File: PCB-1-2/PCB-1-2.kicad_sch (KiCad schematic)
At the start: 4 parts, among them U1 LTC1298IS8_PBF, U2 LTC1451IS8-PBF, U3 HI-3110PSIF, U4 FT231XS-R

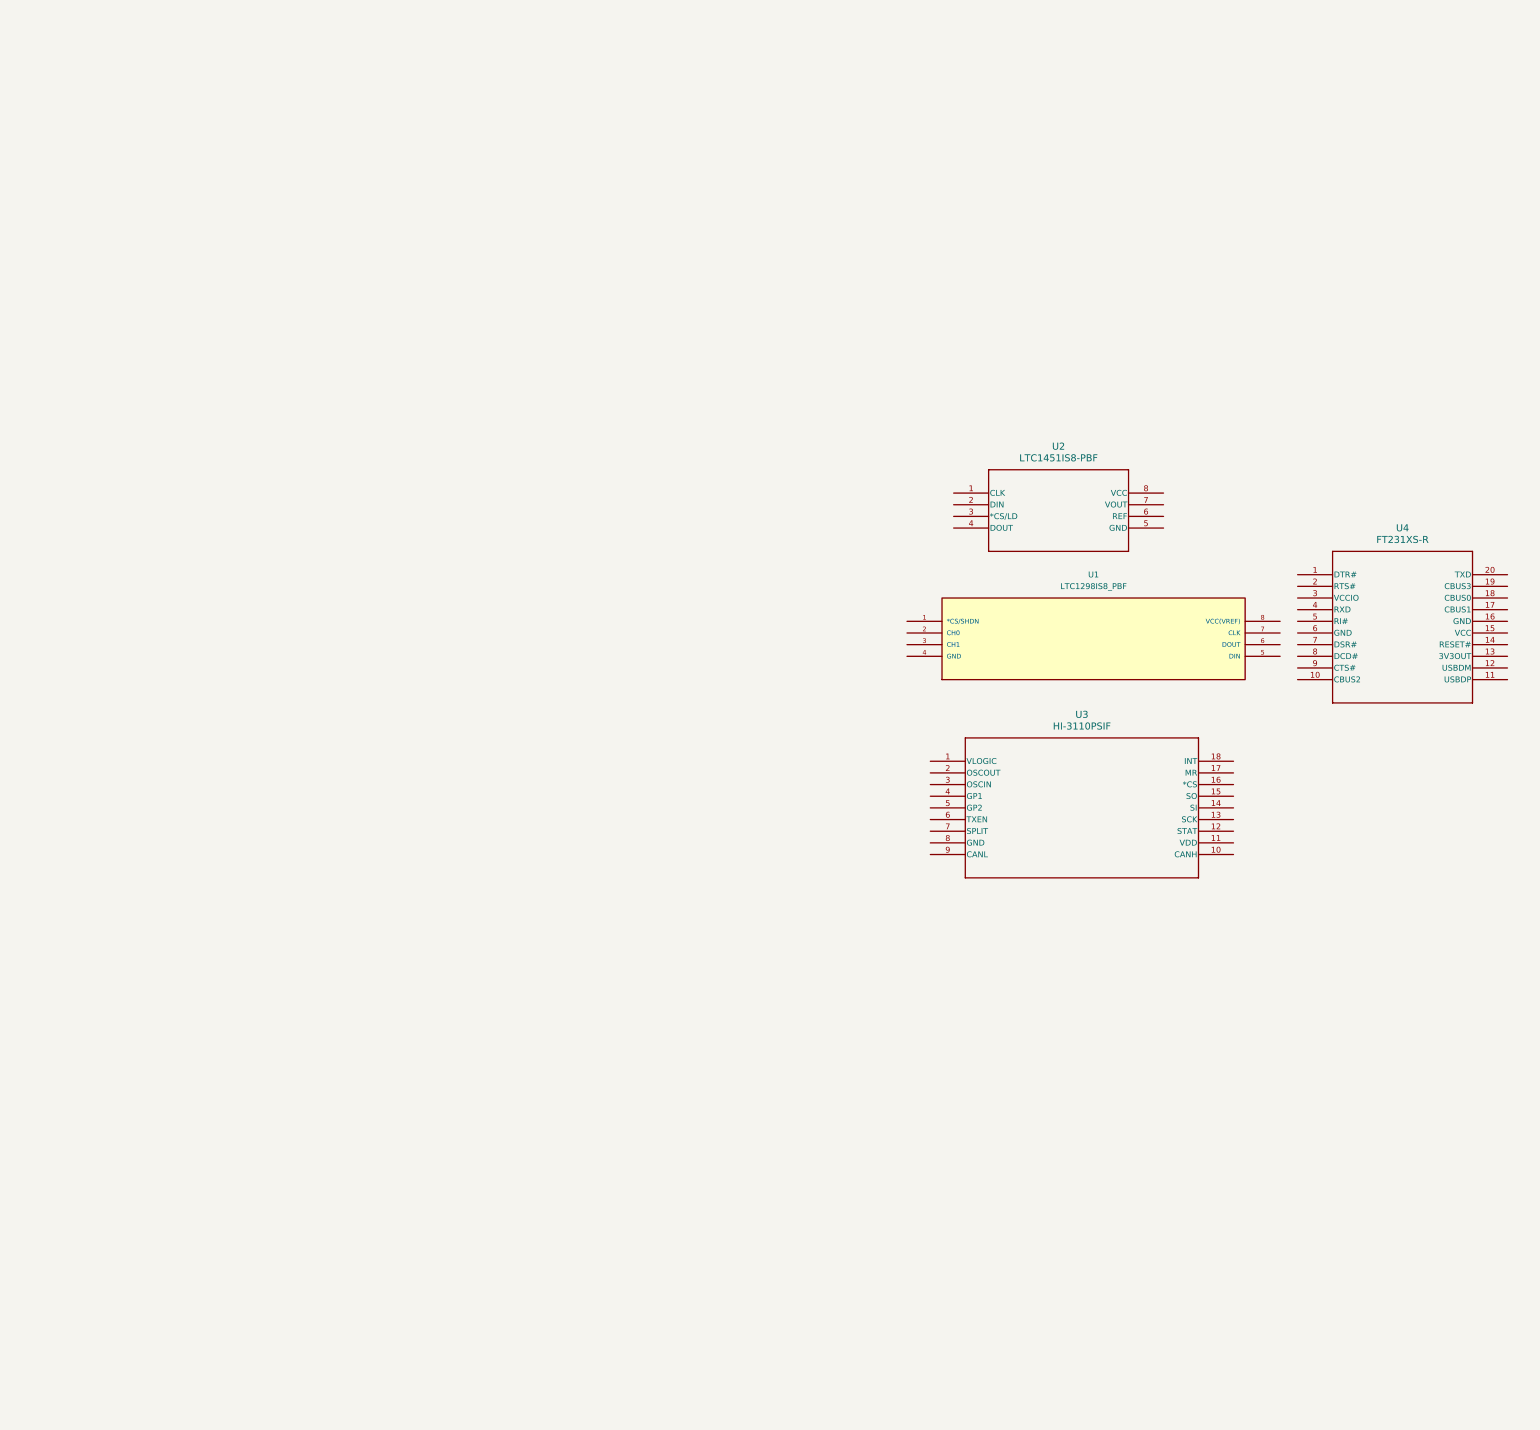
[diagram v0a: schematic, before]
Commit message: Added Schemaitic for ADC, DAC, USB-C. FT231 is still in progress
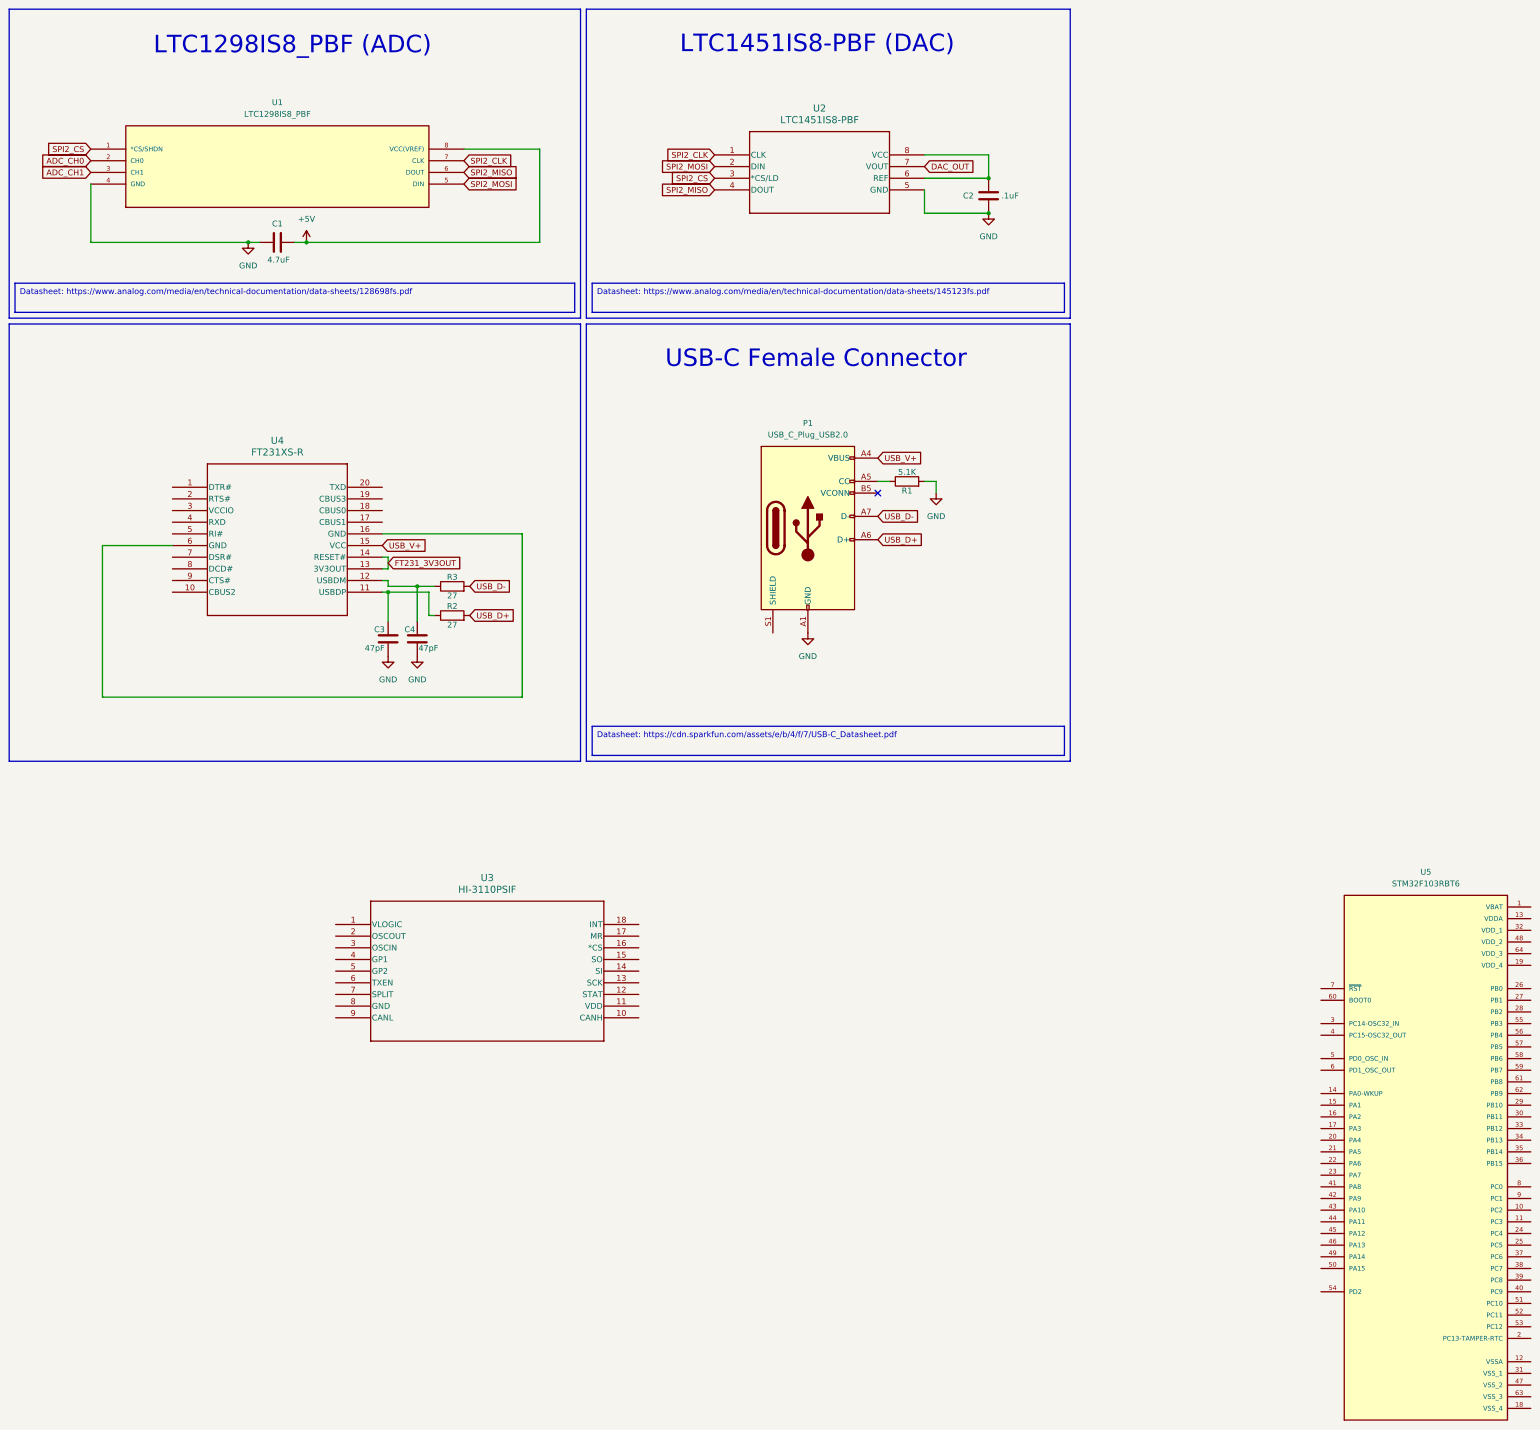
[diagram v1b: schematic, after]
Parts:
- added C1: 4.7uF, symbol Device:C
- added C2: .1uF, symbol Device:C
- added C3, C4: 47pF, symbol Device:C
- added P1: USB_C_Plug_USB2.0, symbol Connector:USB_C_Plug_USB2.0
- added R1: 5.1K, symbol Device:R
- added R2, R3: 27, symbol Device:R
- added U5: STM32F103RBT6, SDII LIB:QFP50P1200X1200X160-64N, symbol STM32F103RBT6:STM32F103RBT6
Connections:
- net SPI2_CLK: now reaches U2.1 (CLK)
- net SPI2_CLK: now also U1.7 (CLK)
- net SPI2_MOSI: now reaches U2.2 (DIN)
- net SPI2_MOSI: now also U1.5 (DIN)
- net SPI2_CS: now reaches U2.3 (*CS/LD)
- net SPI2_CS: now also U1.1 (*CS/SHDN)
- net SPI2_MISO: now reaches U2.4 (DOUT)
- net SPI2_MISO: now also U1.6 (DOUT)
- net GND: now reaches U2.5 (GND)
- net GND: now also U1.4 (GND), C1.1, C2.2, C3.2, C4.2, P1.A1 (GND), P1.A12 (GND), P1.B1 (GND), P1.B12 (GND), R1.2
- net at U2.6 (REF): now also U2.8 (VCC), C2.1
- net DAC_OUT: now reaches U2.7 (VOUT)
- net at U4.11 (USBDP): now also C3.1, R2.1
- net at U4.12 (USBDM): now also C4.1, R3.1
- net FT231_3V3OUT: now reaches U4.13 (3V3OUT)
- net FT231_3V3OUT: now also U4.14 (RESET#)
- net USB_V+: now reaches U4.15 (VCC)
- net USB_V+: now also P1.A4 (VBUS), P1.A9 (VBUS), P1.B4 (VBUS), P1.B9 (VBUS)
- net at U4.16 (GND): now also U4.6 (GND)
- net ADC_CH0: now reaches U1.2 (CH0)
- net ADC_CH1: now reaches U1.3 (CH1)
- net +5V: now reaches U1.8 (VCC(VREF))
- net +5V: now also C1.2
- new net: P1.A5 (CC), R1.1
- new net USB_D+: P1.A6 (D+), R2.2
- new net USB_D-: P1.A7 (D-), R3.2
- no-connect marks 0 -> 1
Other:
- note added: "LTC1298IS8_PBF (ADC)"
- note added: "LTC1451IS8-PBF (DAC)"
- note added: "USB-C Female Connector"
- moved on the sheet: U2, U3, U4

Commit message: Added misc components and added complimentary parts for the MCU
- Added the ADP7104 5v & 3.3V LDO's
- Added the Watchdog and connected it
- Added complimentary components for STM32
- Figured out the desired crystal and complimentary components
- Added Debug port for the ST-Link v3-MINIE
- Assigned footprints for all capacitors and most resistors
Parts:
- added C10, C11, C5, C7, C8, C9: 100nF, Capacitor_SMD:C_0805_2012Metric, symbol Device:C
- added C12: 10uF, Capacitor_SMD:C_0805_2012Metric, symbol Device:C
- added C13, C6: 10nF, Capacitor_SMD:C_0805_2012Metric, symbol Device:C
- added C14, C15: 1uF, Capacitor_SMD:C_0805_2012Metric, symbol Device:C
- added C16, C17: 10pF, Capacitor_SMD:C_0805_2012Metric, symbol Device:C
- added C18, C19: 2.2uF, Capacitor_SMD:C_0805_2012Metric, symbol Device:C
- added C20: .1uF, Capacitor_SMD:C_0805_2012Metric, symbol Device:C
- added FB1: FerriteBead, symbol Device:FerriteBead
- added FB2: 120R, symbol Device:FerriteBead
- added J1: Bus_PCI_Express_x8, Connector_PCBEdge:BUS_PCIexpress_x8, symbol Connector:Bus_PCI_Express_x8
- added J2: ST STDC14 (Debug Connector), FTSH-107-01-F-DV-K-P-TR:SAMTEC_FTSH-107-01-F-DV-K-P-TR, symbol STDC14 (STM32 Debug Conn):FTSH-107-01-F-DV-K-P-TR
- added R10, R5: 100k, Resistor_SMD:R_0805_2012Metric, symbol Device:R
- added R4: 22, symbol Device:R
- added R6, R8: 17.4k, Resistor_SMD:R_0805_2012Metric, symbol Device:R
- added R7: 5.6k, Resistor_SMD:R_0805_2012Metric, symbol Device:R
- added R9: 10k, Resistor_SMD:R_0805_2012Metric, symbol Device:R
- added U6: STWD100YNXWY3F, SDII LIB:SOT23-5_STM, symbol STWD100YNXWY3F (Watchdog):STWD100YNXWY3F
- added U7: ADP7104ACPZ-5V, SDII LIB:CP_8_5_ADI, symbol ADP7104 (LDO):ADP7104ACPZ-3.0-R7
- added U8: ADP7104ACPZ-3.3V, SDII LIB:CP_8_5_ADI, symbol ADP7104 (LDO):ADP7104ACPZ-3.0-R7
- added Y1: 8MHz Crystal, SDII LIB:XTAL_ABM3B-8.000MHZ-10-1-U-T, symbol ABM3B-8MHz (Crystal):ABM3B-8.000MHZ-10-1-U-T
- C1, C2, C3, C4: footprint (none) -> Capacitor_SMD:C_0805_2012Metric
- R1: footprint (none) -> Resistor_SMD:R_0805_2012Metric
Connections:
- net GND is gone; now on net +5V: C1.1, C2.2, C3.2, C4.2, P1.A1 (GND), P1.A12 (GND), P1.B1 (GND), P1.B12 (GND), R1.2, U1.4 (GND), U2.5 (GND)
- net +5V: now also U5.12 (VSSA), U5.18 (VSS_4), U5.31 (VSS_1), U5.47 (VSS_2), U5.60 (BOOT0), U5.63 (VSS_3), C10.1, C11.1, C12.1, C13.2, C14.2, C15.2, C16.2, C17.2, C18.1, C18.2, C19.2, C20.2, C7.1, C8.1, C9.1, J2.05 (GND), J2.07 (GND), J2.11 (GNDDETECT), R5.1, R6.2, R7.1, R9.1, U6.2 (GND), U7.1 (VOUT), U7.3 (GND), U7.6 (GND), U7.9 (EPAD), U8.3 (GND), U8.6 (GND), U8.9 (EPAD), Y1.2 (GND), Y1.4 (GND__1)
- net FT231_3V3OUT: now also U4.3 (VCCIO), C5.1
- net SPI2_CLK: now also U5.34 (PB13)
- net SPI2_MISO: now also U5.35 (PB14)
- net SPI2_MOSI: now also U5.36 (PB15)
- net USB_V+: now also C6.2, FB1.2; no longer U4.15 (VCC)
- net +3.3V: now reaches U5.1 (VBAT)
- net +3.3V: now also U5.13 (VDDA), U5.19 (VDD_4), U5.32 (VDD_1), U5.48 (VDD_2), U5.64 (VDD_3), C10.2, C11.2, C12.2, C13.1, C14.1, C15.1, C19.1, C7.2, C8.2, C9.2, FB2.1, FB2.2, J2.03 (VCC), R10.1, R8.2, U6.5 (VCC), U8.1 (VOUT)
- net SWDIO: now reaches U5.46 (PA13)
- net SWDIO: now also R4.2
- net SWCLK: now reaches U5.49 (PA14)
- net SWCLK: now also J2.06 (SWCLK)
- net at U5.5 (PD0_OSC_IN): now also C16.1, Y1.1
- net SWO: now reaches U5.55 (PB3)
- net SWO: now also J2.08 (SWO)
- net at U5.6 (PD1_OSC_OUT): now also C17.1, Y1.3
- net MCU_NRST: now reaches U5.7 (~{RST})
- net MCU_NRST: now also C20.1, J2.12 (NRST), U6.1 (*WDO)
- net at U4.16 (GND), U4.6 (GND): now also C5.2, C6.1
- new net: R5.2, U7.7 (PG)
- new net: R8.1, R9.2, U8.2 (SENSE/ADJ)
- new net: R10.2, U8.7 (PG)
- new net: J2.04 (SWDIO), R4.1
- new net: R6.1, R7.2, U7.2 (SENSE/ADJ)
- new net: FB1.1, U4.15 (VCC)
- new net: J1.A10 (+3.3V), J1.A9 (+3.3V), J1.B8 (+3.3V)
- new net: J1.A12 (GND), J1.A15 (GND), J1.A18 (GND), J1.A20 (GND), J1.A23 (GND), J1.A24 (GND), J1.A27 (GND), J1.A28 (GND), J1.A31 (GND), J1.A34 (GND), J1.A37 (GND), J1.A38 (GND), J1.A4 (GND), J1.A41 (GND), J1.A42 (GND), J1.A45 (GND), J1.A46 (GND), J1.A49 (GND), J1.B13 (GND), J1.B16 (GND), J1.B18 (GND), J1.B21 (GND), J1.B22 (GND), J1.B25 (GND), J1.B26 (GND), J1.B29 (GND), J1.B32 (GND), J1.B35 (GND), J1.B36 (GND), J1.B39 (GND), J1.B4 (GND), J1.B40 (GND), J1.B43 (GND), J1.B44 (GND), J1.B47 (GND), J1.B49 (GND), J1.B7 (GND)
- new net: J1.A2 (+12V), J1.A3 (+12V), J1.B1 (+12V), J1.B2 (+12V), J1.B3 (+12V)
- new net V+_FROM_PCIE: U7.5 (EN/UVLO), U7.8 (VIN), U8.5 (EN/UVLO), U8.8 (VIN)
- new net WD_EN: U6.3 (*EN)
- new net WD_WDI: U6.4 (WDI)
- no-connect marks 1 -> 5
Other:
- note added: "ADP7104 3.3V LDO"
- note added: "ADP7104 5V LDO"
- moved on the sheet: C1, C3, C4, P1, R1, R2, R3, U3, U4, U5

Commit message: Reformatted the schematic to look cleaner
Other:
- note added: "STDC14 Serial Wire Debug Connector"
- note added: "STWD100 Watchdog"
- moved on the sheet: C10, C11, C12, C13, C14, C15, C16, C17, C20, C7, C8, C9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

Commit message: Updated a few things
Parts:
- removed U7: ADP7104ACPZ-5V, SDII LIB:CP_8_5_ADI, symbol ADP7104 (LDO):ADP7104ACPZ-3.0-R7
- removed U8: ADP7104ACPZ-3.3V, SDII LIB:CP_8_5_ADI, symbol ADP7104 (LDO):ADP7104ACPZ-3.0-R7
- added U7, U9: ADP7104ACPZ-R7, CP_8_5_ADI, symbol ADP7104 (LDO):ADP7104ACPZ-R7
- C12: value 10uF -> 4.7uF
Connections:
- net +3.3V: now also U7.1 (VOUT)
- net +5V: now also U7.3 (GND), U7.5 (EN/UVLO), U7.6 (GND), U7.8 (VIN), U7.9 (EPAD), U9.1 (VOUT), U9.3 (GND), U9.5 (EN/UVLO), U9.6 (GND), U9.8 (VIN), U9.9 (EPAD)
- net at R5.2: now also U9.7 (PG)
- net at R8.1, R9.2: now also U7.2 (SENSE/ADJ)
- net at R10.2: now also U7.7 (PG)
- net OSC_OUT: now reaches C17.1, U5.6 (PD1_OSC_OUT), Y1.3
- net SPI2_NSS: now reaches U5.33 (PB12)
- net OSC_IN: now reaches C16.1, U5.5 (PD0_OSC_IN), Y1.1
- net at R6.1, R7.2: now also U9.2 (SENSE/ADJ)
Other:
- note added: "ADD NET-LABELS FOR ROUTING PURPOSES"
- note added: "Vout = 1.22(1 + (17.4k/10k)) = 3.34V {See ADP7104-16}"
- note added: "Vout = 1.22(1 + (17.4k/5.6k)) = 5.01V {See ADP7104-16}"
- company: (none) -> Kansas State University
- title: (none) -> 0.1
- moved on the sheet: C10, C11, C12, C13, C14, C15, C16, C17, C18, C19, C20, C3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

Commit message: Finished adding connections to the FTDI chip
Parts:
- added D1, D2, D3, D4: LED, symbol Device:LED
- added R11, R12: R, symbol Device:R
- added R13, R14: 270, symbol Device:R
- C18, C19: value 2.2uF -> 4.7uF
- U7: value ADP7104ACPZ-R7 -> ADP7104ACPZ-R7 (v3.3)
- U9: value ADP7104ACPZ-R7 -> ADP7104ACPZ-R7 (5v)
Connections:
- net +3.3V: now also U3.1 (VLOGIC)
- net +5V: now also U3.11 (VDD); no longer C1.2, C10.1, C11.1, C12.1, C13.2, C14.2, C15.2, C16.2, C17.2, C18.2, C19.2, C2.2, C20.2, C3.2, C4.2, C7.1, C8.1, C9.1, J2.05 (GND), J2.07 (GND), J2.11 (GNDDETECT), P1.A1 (GND), P1.A12 (GND), P1.B1 (GND), P1.B12 (GND), R1.2, R7.1, R9.1, U1.4 (GND), U2.5 (GND), U5.12 (VSSA), U5.18 (VSS_4), U5.31 (VSS_1), U5.47 (VSS_2), U5.60 (BOOT0), U5.63 (VSS_3), U6.2 (GND), U7.3 (GND), U7.5 (EN/UVLO), U7.6 (GND), U7.8 (VIN), U7.9 (EPAD), U9.3 (GND), U9.5 (EN/UVLO), U9.6 (GND), U9.8 (VIN), U9.9 (EPAD), Y1.2 (GND), Y1.4 (GND__1)
- net FT231_3V3OUT: now also R13.1, R14.1
- net GND: now reaches C5.2, C6.1, U4.16 (GND), U4.6 (GND)
- net GND: now also C1.2, C10.1, C11.1, C12.1, C13.2, C14.2, C15.2, C16.2, C17.2, C18.2, C19.2, C2.2, C20.2, C3.2, C4.2, C7.1, C8.1, C9.1, J2.05 (GND), J2.07 (GND), J2.11 (GNDDETECT), P1.A1 (GND), P1.A12 (GND), P1.B1 (GND), P1.B12 (GND), R1.2, R7.1, R9.1, U1.4 (GND), U2.5 (GND), U3.8 (GND), U5.12 (VSSA), U5.18 (VSS_4), U5.31 (VSS_1), U5.47 (VSS_2), U5.60 (BOOT0), U5.63 (VSS_3), U6.2 (GND), U7.3 (GND), U7.6 (GND), U7.9 (EPAD), U9.3 (GND), U9.6 (GND), U9.9 (EPAD), Y1.2 (GND), Y1.4 (GND__1)
- net at U3.4 (GP1): now also D1.2 (A)
- net at U3.5 (GP2): now also D2.2 (A)
- net USART_RXLED: now reaches U4.10 (CBUS2)
- net USART_RXLED: now also D3.1 (K)
- net at U4.17 (CBUS1): now also D4.1 (K)
- net USART2_RX: now reaches U4.20 (TXD)
- net USART2_TX: now reaches U4.4 (RXD)
- net USB_V+ renamed USB_VDD
- new net: D3.2 (A), R13.2
- new net USART_TXLED: D4.2 (A), R14.2
- new net V+_FROM_PCIE: U7.5 (EN/UVLO), U7.8 (VIN), U9.5 (EN/UVLO), U9.8 (VIN)
- no-connect marks 5 -> 13
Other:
- note added: "FT231XS-R UART to USB"
- note added: "Need to add ARINC 429 Chip"
- moved on the sheet: C1, C3, C4, C5, C6, FB1, J1, P1, R1, R2, R3, U3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

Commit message: Updated schematic to add the RTD and Transducer signal conditioning
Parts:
- added C21, C25: 10nF, symbol Device:C
- added C22: 332nF, symbol Device:C
- added C23: 0.015uF, symbol Device:C
- added C24, C28: 0.1uF, symbol Device:C
- added C26: 1uF, symbol Device:C
- added C27: 10uF, symbol Device:C
- added C29: 400pF, symbol Device:C
- added C30, C31: 40pF, symbol Device:C
- added J3: USB4105-GF-A, SDII LIB:GCT_USB4105-GF-A, symbol USB-C Connector:USB4105-GF-A
- added R15: 10.7k, symbol Device:R
- added R16, R19: 1.13k, symbol Device:R
- added R17, R18: 1M, symbol Device:R
- added R20: 750, symbol Device:R
- added R21: 5.5k, symbol Device:R
- added R22, R23: 1k, symbol Device:R
- added R24: 2.5k, symbol Device:R
- added U10: INA827AIDGKR, SDII LIB:DGK8_TEX, symbol INA827AIDGKR (Instrumentation Amp):INA827AIDGKR
- added U11: LTC1250CS8-PBF, SDII LIB:SO-8_S_LIT, symbol LTC1250 (Zero Drift Bridge Amp):LTC1250CS8-PBF
- added U12: REF3425MDBVTEP, SDII LIB:SOT-23-6_TEX, symbol REF3425 (Fixed VRef 2.5v):REF3425MDBVTEP
- added U13: HI-3585APQI, SDII LIB:QFP80P1390X1390X150-44N, symbol HI-3585APQI (ARINC 429):HI-3585APQI
- added U8: OPA2187IDGKR, SDII LIB:DGK8_TEX, symbol OPA21B7IDGKR (OpAmp):OPA2187IDGKR
- J2: footprint FTSH-107-01-F-DV-K-P-TR:SAMTEC_FTSH-107-01-F-DV-K-P-TR -> SDII LIB:SAMTEC_FTSH-107-01-F-DV-K-P-TR
- U7, U9: footprint CP_8_5_ADI -> SDII LIB:CP_8_5_ADI
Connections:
- net +5V: now also C24.2, C26.1, C28.1, R17.1, U10.8 (VS+), U11.7 (V+), U12.3 (ENABLE), U12.4 (IN), U8.8 (V+)
- net ADC_CH0: now also U10.7 (VOUT)
- net ADC_CH1: now also C25.2, R19.1, U8.7 (OUT_B)
- net GND: now also C21.2, C22.2, C23.2, C24.1, C26.2, C28.2, C30.2, C31.2, R18.2, R24.2, U10.5 (VS-), U10.6 (REF), U11.4 (V-), U12.1 (GND_F), U12.2 (GND_S), U8.4 (V-)
- net SWO: no longer U5.55 (PB3)
- net USB_VDD: now also J3.A4_B9 (VBUS)
- net at C2.1, U2.8 (VCC): no longer U2.6 (REF)
- new net: C23.1, R17.2, R18.1, U8.5 (+IN_B)
- new net: C21.1, R15.2, U8.3 (+IN_A)
- new net: C29.1, C30.1, R22.2, U10.1 (IN-)
- new net: C29.2, C31.1, R23.2, U10.4 (IN+)
- new net: R21.2, U10.2 (RG)
- new net: R21.1, U10.3 (RG)
- new net: J3.A6 (DP1), J3.B6 (DP2)
- new net: J3.A7 (DN1), J3.B7 (DN2)
- new net: C22.1, R16.2, R19.2, R20.1
- new net: C27.1, U11.3 (+IN), U12.5 (OUT_S), U12.6 (OUT_F)
- new net: C25.1, R20.2, U8.6 (-IN_B)
- new net: R16.1, U8.1 (OUT_A), U8.2 (-IN_A)
- new net RTD+: R23.1, U11.6 (OUT)
- new net RTD-: R22.1, R24.1, U11.2 (-IN)
- new net Transducer+: R15.1
- no-connect marks 13 -> 14
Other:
- note added: "Do we need a bypass cap for the enable pin?"
- note added: "Has an internal REF of 2.048v"
- note added: "RTD Signal Conditioning"
- note added: "See REF3425 Datasheet for schematic and layout recomendations"
- note added: "Transducer Signal Conditioning"
- moved on the sheet: C10, C11, C12, C13, C14, C15, C16, C17, C20, C7, C8, C9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

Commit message: Added used pins to MCU, also semi wired up 429
Still need to look a the devboard schematic for the 429 and use its wiring
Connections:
- net SPI2_NSS is gone; now on net SPI2_CS: U5.33 (PB12)
- net +3.3V: now also U13.40 (VDD)
- net +5V: now also U13.38 (V_POS)
- net GND: now also U13.17 (GND)
- net SPI2_CS: now also U13.9 (~{CS})
- net SPI2_MISO: now also U13.20 (SO)
- net SPI2_MOSI: now also U13.8 (SI)
- net USART2_RX: now also U5.17 (PA3)
- net USART2_TX: now also U5.16 (PA2)
- net WD_EN: now also U5.15 (PA1)
- net WD_WDI: now also U5.14 (PA0-WKUP)
- net DISCRETE_OUTPUT_3: now reaches U5.10 (PC2)
- net DISCRETE_OUTPUT_4: now reaches U5.11 (PC3)
- net SPI1_CS: now reaches U5.20 (PA4)
- net SPI1_SCK: now reaches U5.21 (PA5)
- net SPI1_MISO: now reaches U5.22 (PA6)
- net SPI1_MOSI: now reaches U5.23 (PA7)
- net DISCRETE_OUTPUT_5: now reaches U5.24 (PC4)
- net DISCRETE_OUTPUT_6: now reaches U5.25 (PC5)
- net ARINC_429_CLK: now reaches U5.26 (PB0)
- net ARINC_429_CLK: now also U13.19 (ACLK)
- net HW_ID_1: now reaches U5.27 (PB1)
- net HW_ID_2: now reaches U5.28 (PB2)
- net DISCRETE_INPUT_1: now reaches U5.37 (PC6)
- net DISCRETE_INPUT_2: now reaches U5.38 (PC7)
- net DISCRETE_INPUT_3: now reaches U5.39 (PC8)
- net DISCRETE_INPUT_4: now reaches U5.40 (PC9)
- net USART1_TX: now reaches U5.42 (PA9)
- net USART1_TX: now also J2.14 (VCP_TX)
- net USART1_RX: now reaches U5.43 (PA10)
- net USART1_RX: now also J2.13 (VCP_RX)
- net DISCRETE_INPUT_5: now reaches U5.51 (PC10)
- net DISCRETE_INPUT_6: now reaches U5.52 (PC11)
- net HW_ID_3: now reaches U5.55 (PB3)
- net DISCRETE_OUTPUT_1: now reaches U5.8 (PC0)
- net DISCRETE_OUTPUT_2: now reaches U5.9 (PC1)
- net SPI2_SCK: now reaches U13.15 (SCK)
- net 429_IN-: now reaches U13.3 (RINB)
- net -5V: now reaches U13.30 (V_NEG)
- net 429_OUT-: now reaches U13.32 (BOUT37)
- net 429_OUT+: now reaches U13.35 (AOUT37)
- net 429_IN+: now reaches U13.43 (RINA)
- net SWO: no longer names the net of J2.08 (SWO)
- no-connect marks 14 -> 22
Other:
- note added: "3x Toggle Switches 3x Momentary Switches"
- note added: "Add these if there are extra pins go high when TX and RX buffer are empty)"
- note added: "HI-3585 (ARINC 429)"
- note added: "Master Reset (ADD IF EXTRA PINS)"
- note added: "Need a -5v LDO for the ARINC429 chip"
- note added: "Need to use SPI1 for ARINC 825"
- note removed: "Need to add ARINC 429 Chip"
- moved on the sheet: C10, C11, C12, C13, C14, C15, C16, C17, C20, C7, C8, C9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
